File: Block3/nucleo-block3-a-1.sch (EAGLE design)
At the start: 21 parts, among them J1 DSUB-9-RIGHT-ANGLE, J2 DSUB-9-RIGHT-ANGLE, J3 DSUB-9-RIGHT-ANGLE, U1 TC4428ACOA, U2 TC4428ACOA, U3 TC4428ACOA

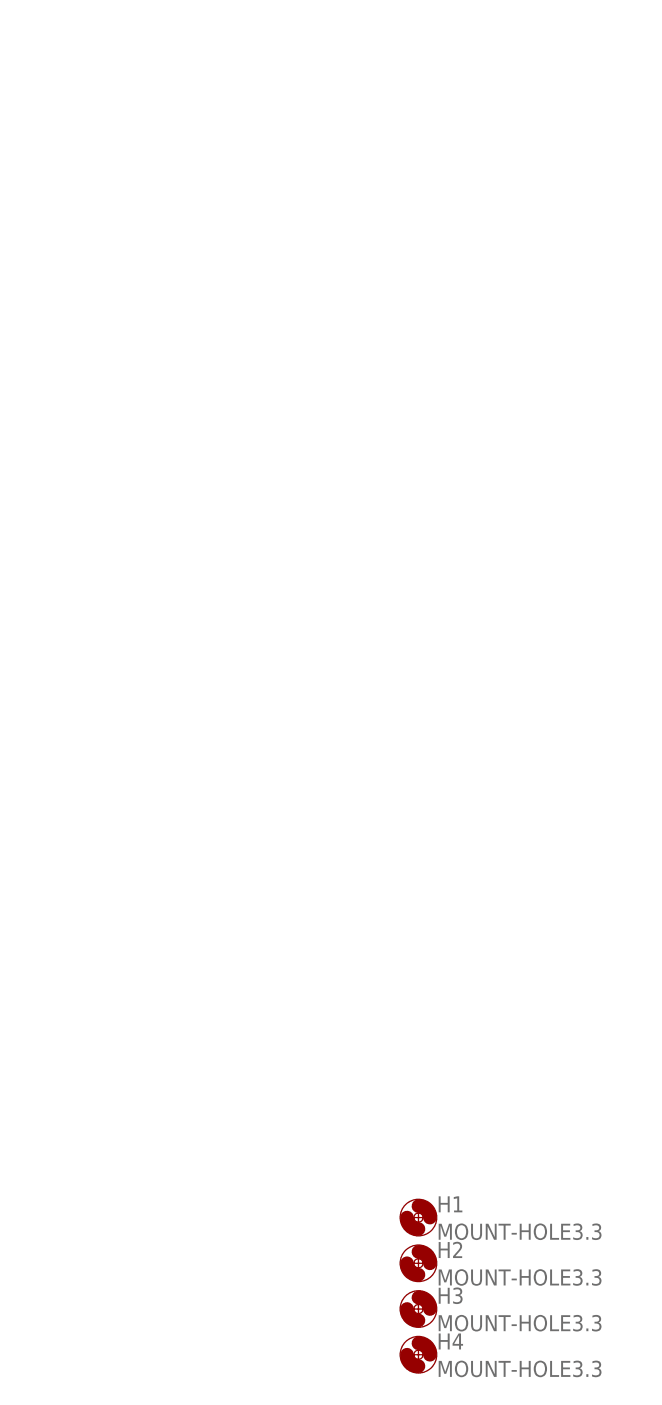
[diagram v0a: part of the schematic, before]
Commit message: Adds morpho header. Lays out connectors.
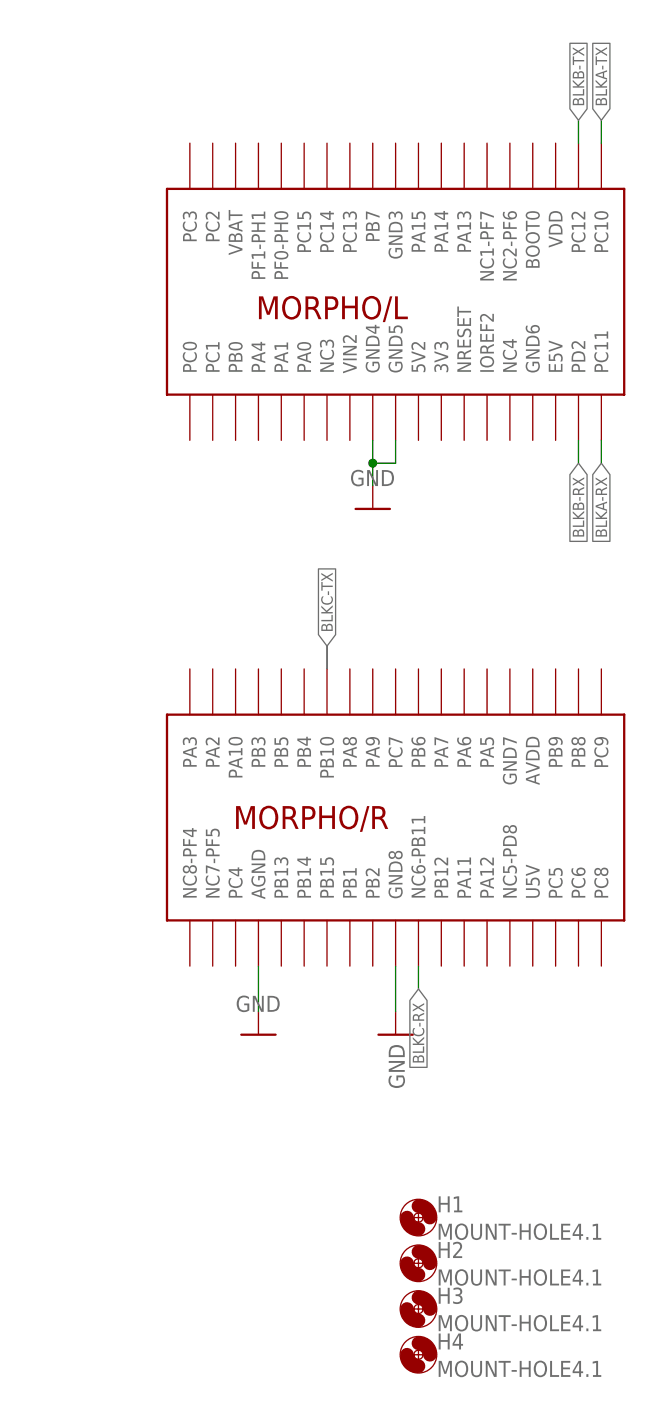
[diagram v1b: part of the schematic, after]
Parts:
- added G1: NUCLEO_64_GENERIC, eagleparts:NUCLEO_64_GENERIC
- H1, H2, H3, H4: value MOUNT-HOLE3.3 -> MOUNT-HOLE4.1; device holes:MOUNT-HOLE3.3 -> holes:MOUNT-HOLE4.1
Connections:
- net BLKA-RX: now also G1.PC11
- net BLKA-TX: now also G1.PC10
- net BLKB-RX: now also G1.PD2
- net BLKB-TX: now also G1.PC12
- net BLKC-RX: now also G1.NC6-PB11
- net BLKC-TX: now also G1.PB10
- net GND: now also G1.AGND, G1.GND4, G1.GND5, G1.GND8

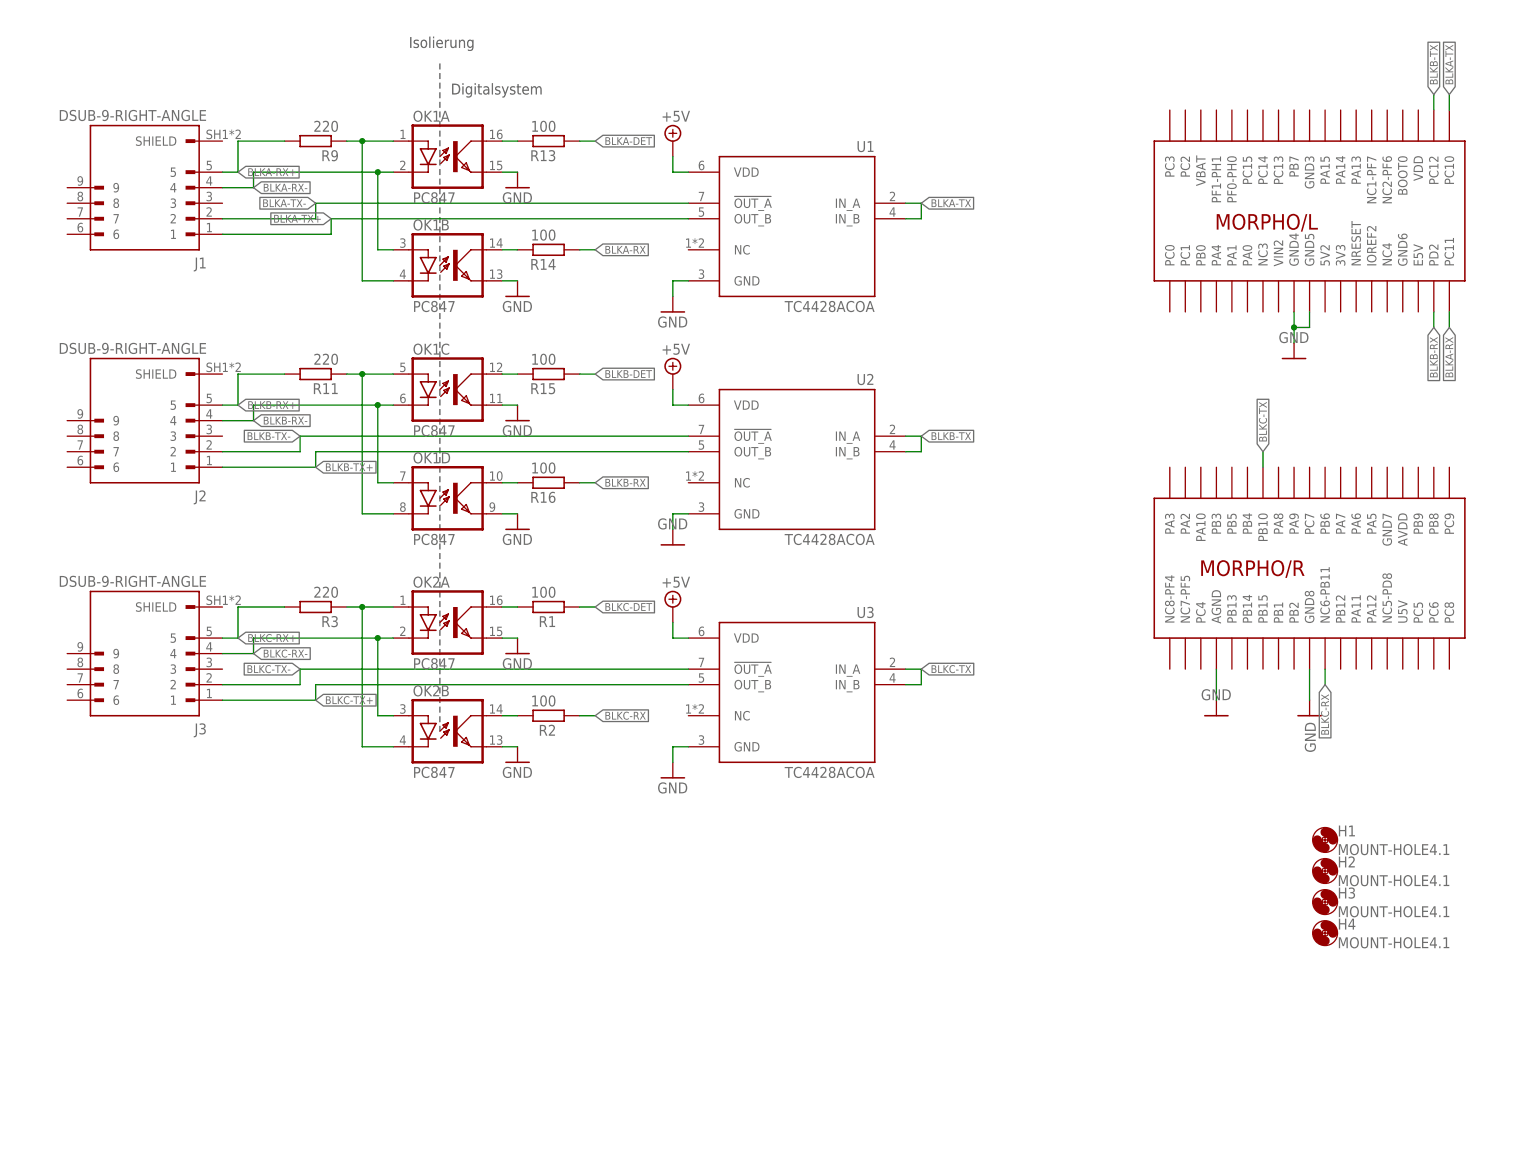
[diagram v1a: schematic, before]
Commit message: Adds LN circuitry.
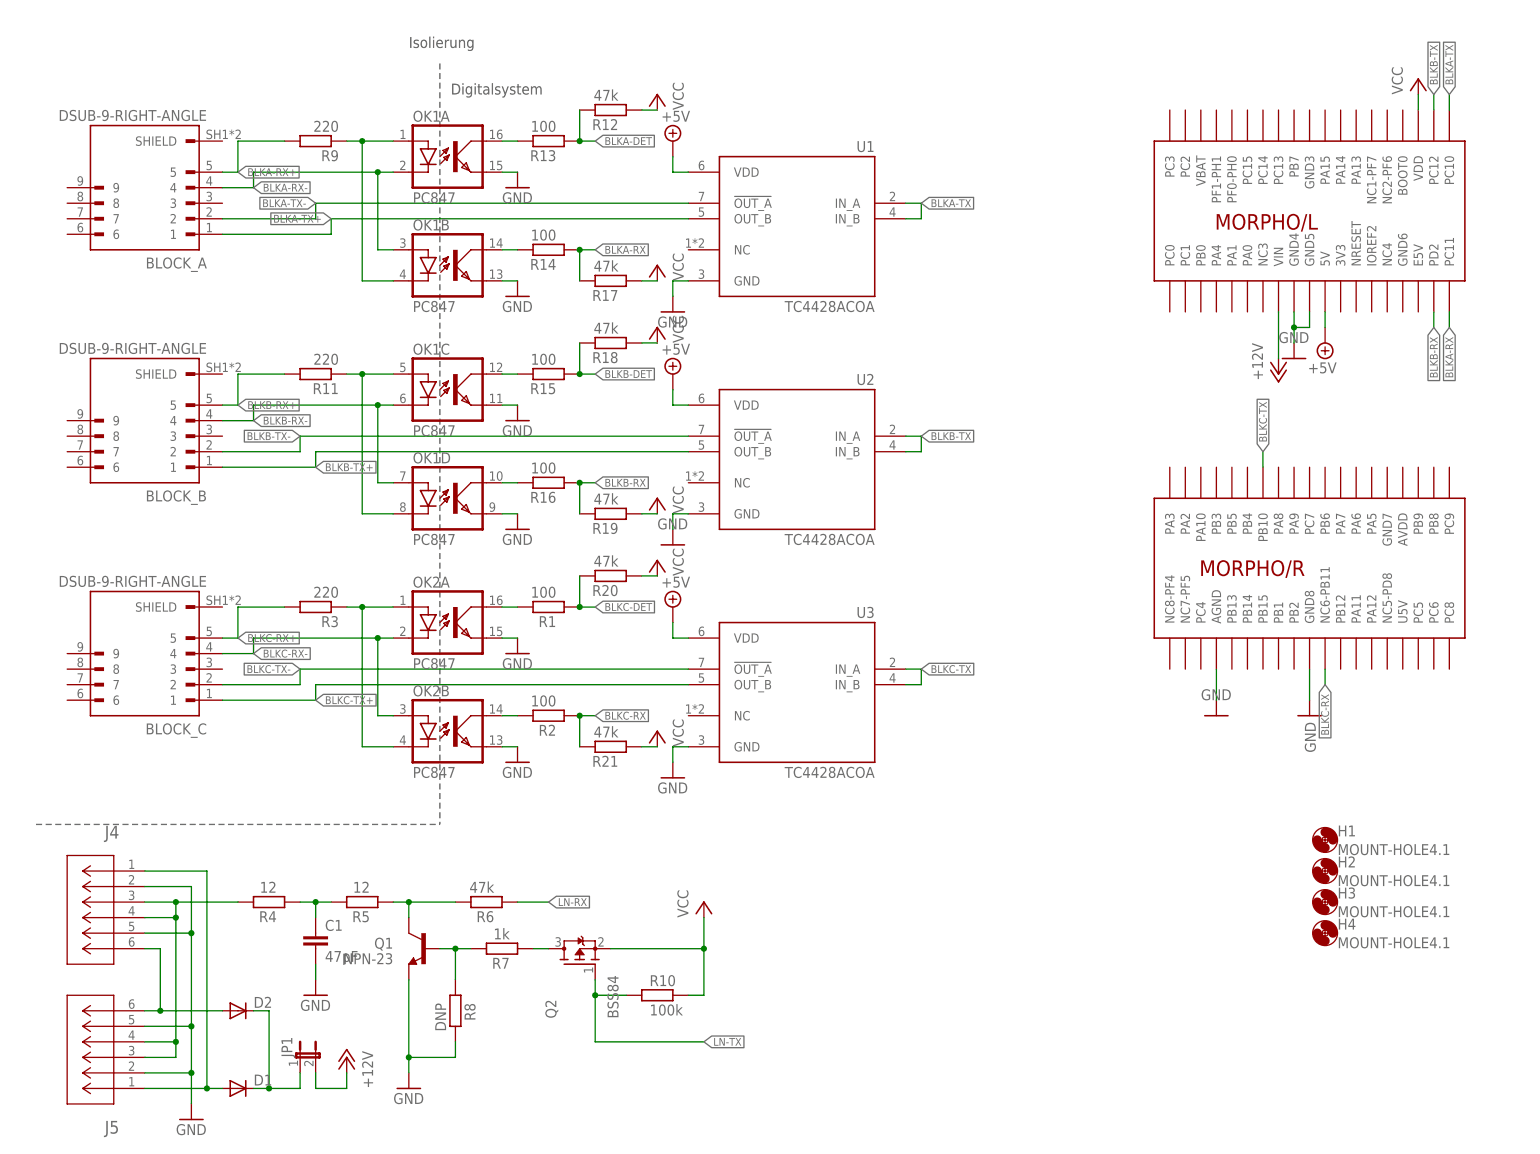
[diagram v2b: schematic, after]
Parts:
- added C1: 47pF, rcl:C-EUC0805
- added D1, D2: DIODEDO-214AA-NODOC, trainlib:DIODEDO-214AA-NODOC
- added J4, J5: MODJACK-6P6CCONN_SS-90000-003_STW, eagleparts:MODJACK-6P6CCONN_SS-90000-003_STW
- added JP1: (no value), jumper:JP1E
- added Q1: NPN-23, eagleparts:NPN-23
- added Q2: BSS84, eagleparts:BSS84
- added R10: 100k, rcl:R-EU_R0805
- added R12, R17, R18, R19, R20, R21, R6: 47k, rcl:R-EU_R0805
- added R4, R5: 12, rcl:R-EU_R0805
- added R7: 1k, rcl:R-EU_R0805
- added R8: DNP, rcl:R-EU_R0805
- renumbered J1 to BLOCK_A, J2 to BLOCK_B, J3 to BLOCK_C
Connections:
- new net +12V: G1.VIN, JP1.2
- new net LN-RX: R6.1
- new net LN-TX: Q2.G, R10.1
- new net N$10: Q2.D, R7.1
- new net N$11: Q1.B, R7.2, R8.1
- new net N$4: D2.A, J4.6, J5.6
- new net N$5: C1.1, R4.1, R5.2
- new net N$6: D1.A, J4.1, J5.1
- new net N$7: J4.3, J4.4, J5.3, J5.4, R4.2
- new net N$8: D1.C, D2.C, JP1.1
- new net N$9: Q1.C, R5.1, R6.2
- new net VCC: G1.VDD, Q2.S, R10.2, R12.1, R17.1, R18.1, R19.1, R20.1, R21.1
- net +5V: now also G1.5V
- net BLKA-DET: now also R12.2
- net BLKA-RX: now also R17.2
- net BLKB-DET: now also R18.2
- net BLKB-RX: now also R19.2
- net BLKC-DET: now also R20.2
- net BLKC-RX: now also R21.2
- net GND: now also C1.2, J4.2, J4.5, J5.2, J5.5, Q1.E, R8.2

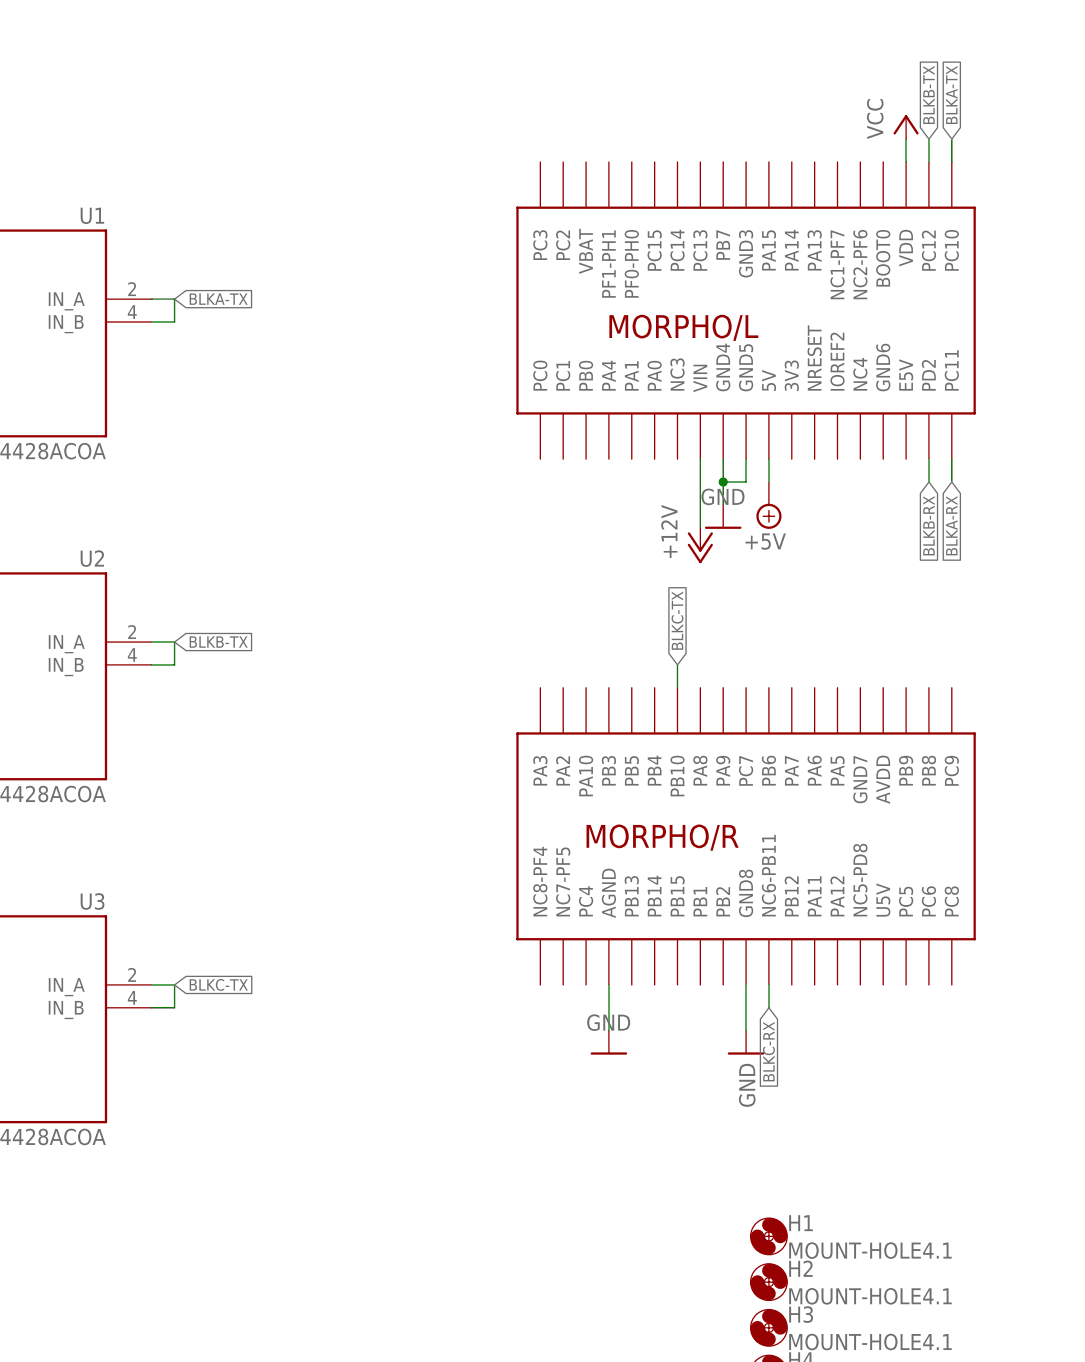
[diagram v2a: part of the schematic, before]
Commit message: Adds addressable LEDs.
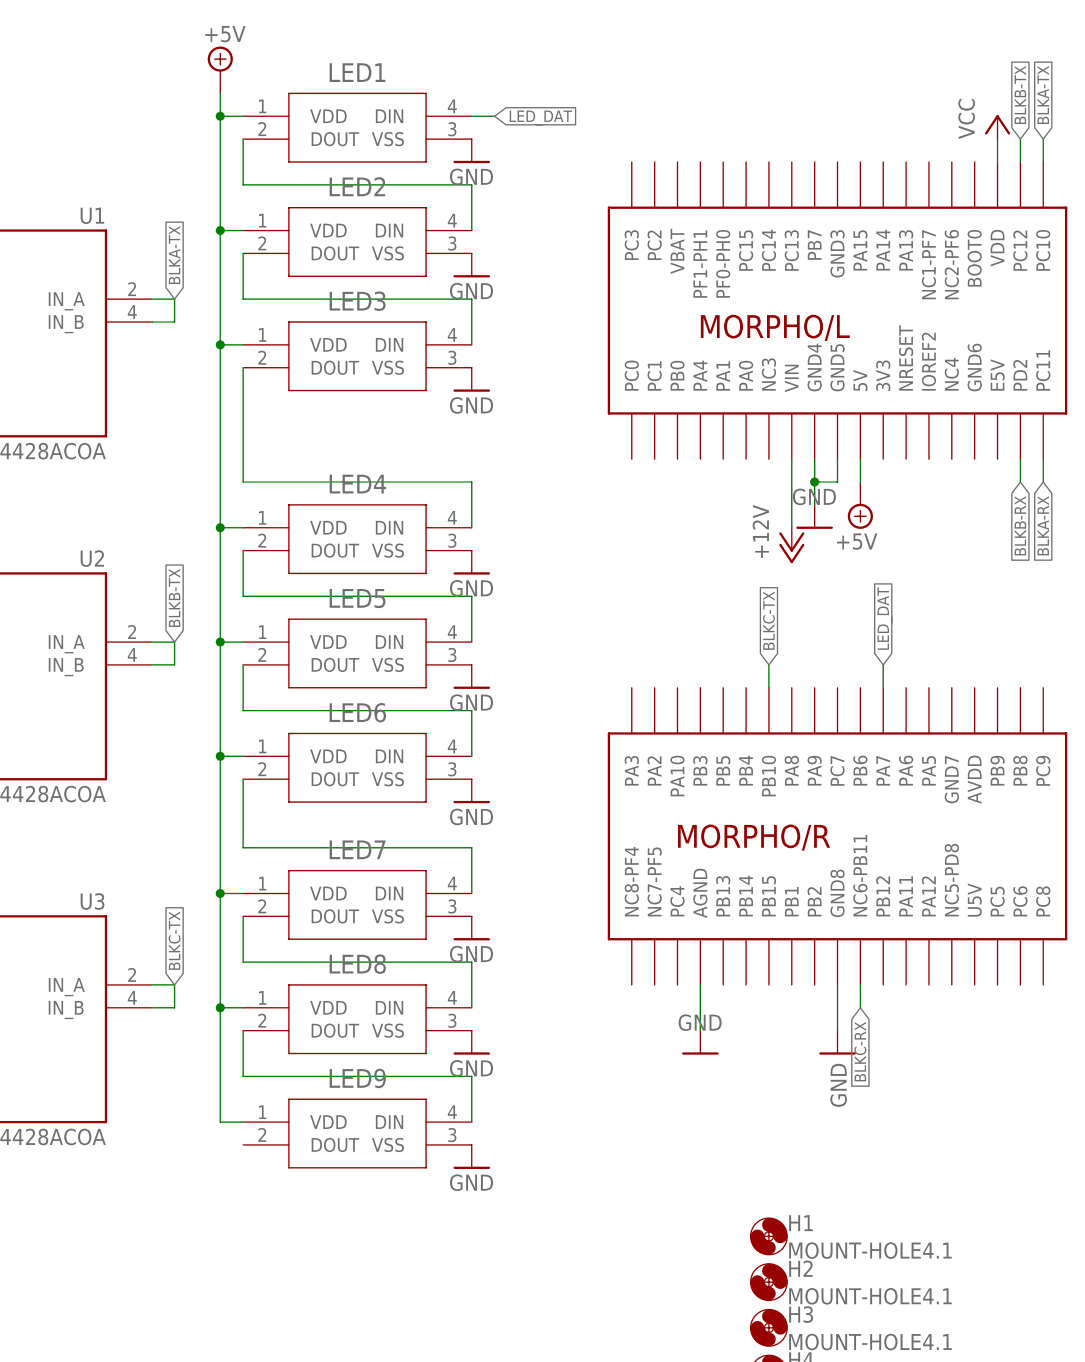
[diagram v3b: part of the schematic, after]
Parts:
- added LED1, LED2, LED3, LED4, LED5, LED6, LED7, LED8, LED9: LED-2812BCOM-16347_SPK-M, eagleparts:LED-2812BCOM-16347_SPK-M
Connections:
- new net LED_DAT: G1.PA7, LED1.DIN
- new net N$12: LED1.DOUT, LED2.DIN
- new net N$13: LED2.DOUT, LED3.DIN
- new net N$14: LED3.DOUT, LED4.DIN
- new net N$15: LED4.DOUT, LED5.DIN
- new net N$16: LED5.DOUT, LED6.DIN
- new net N$17: LED6.DOUT, LED7.DIN
- new net N$18: LED7.DOUT, LED8.DIN
- new net N$19: LED8.DOUT, LED9.DIN
- net +5V: now also LED1.VDD, LED2.VDD, LED3.VDD, LED4.VDD, LED5.VDD, LED6.VDD, LED7.VDD, LED8.VDD, LED9.VDD
- net GND: now also LED1.VSS, LED2.VSS, LED3.VSS, LED4.VSS, LED5.VSS, LED6.VSS, LED7.VSS, LED8.VSS, LED9.VSS
